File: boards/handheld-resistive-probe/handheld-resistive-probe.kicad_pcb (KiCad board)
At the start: 4 copper layers, 75 x 8 mm, 4 parts, among them J1 Conn_Coaxial, J2 Conn_01x01

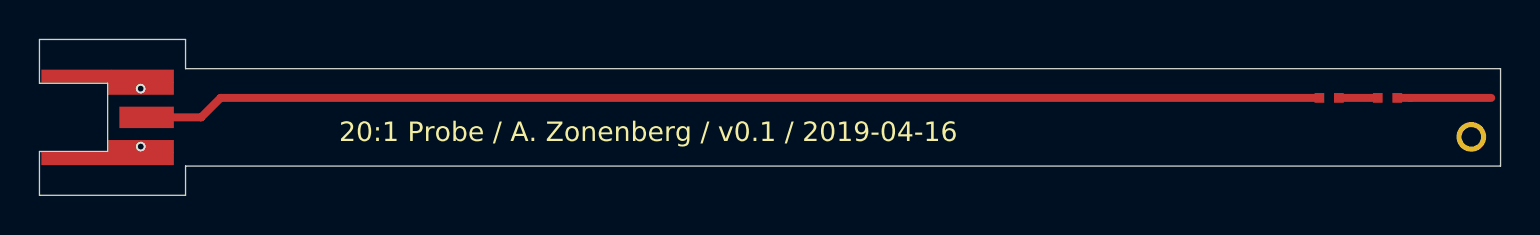
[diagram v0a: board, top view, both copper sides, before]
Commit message: handheld-resistive-probe: respin with coplanar waveguide PCB layout
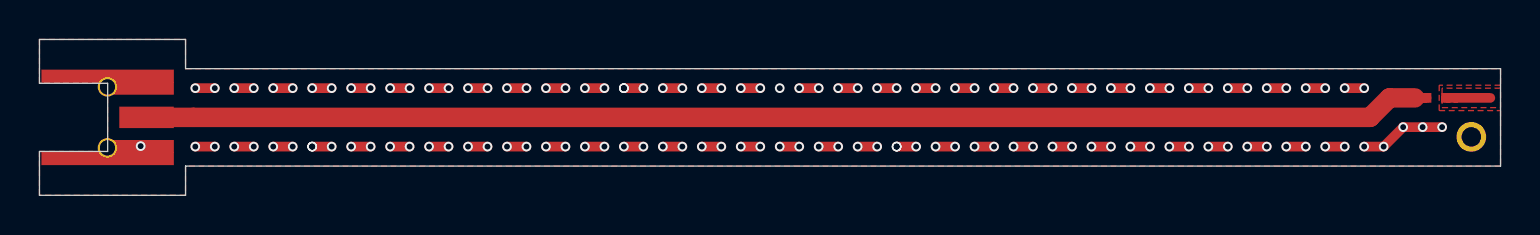
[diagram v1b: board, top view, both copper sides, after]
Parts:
- removed R2: 475, azonenberg_pcb:EIA_0402_RES_NOSILK
- R1: value 475 -> 953
- moved R1 5.50 mm to (86.7, 23.5)
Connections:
- net Net-(J1-Pad1) renamed /SIGNAL
- R1 pad 1: Net-(R1-Pad1) -> /PROBE
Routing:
- net /GND: track 76.4 -> 139.1 mm, vias 2 -> 130
- net /SIGNAL: track 60.6 -> 66.1 mm
- net Net-(R2-Pad1): track 4.82 -> 0.00 mm
- net /PROBE: track 0.00 -> 2.27 mm
- net Net-(R1-Pad1): track 2.00 -> 0.00 mm
- added copper zone on F.Cu, net /GND
- added copper zone on In2.Cu, net /GND
- added copper zone on F.Cu, net /PROBE
- removed copper zone on In1.Cu, net /GND
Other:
- net class Default: clearance 0.25 -> 0.125; trace_width 0.41 -> 1
- rule trace_clearance: 0.25 -> 0.125
- board text added: "20:1 Probe / A. Zonenberg / v0.2 / 2019-05-09"
- board text removed: "20:1 Probe / A. Zonenberg / v0.1 / 2019-04-16"

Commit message: New rev of handheld-resistive-probe with five resistors to reduce parasitics
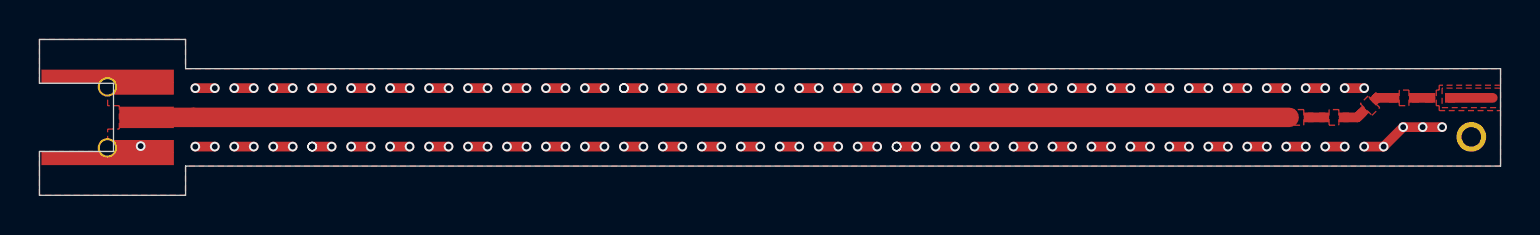
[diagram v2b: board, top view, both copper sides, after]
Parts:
- added R2: 100, azonenberg_pcb:EIA_0402_RES_NOSILK, F.Cu at (81.5, 24.5)
- added R3: 100, azonenberg_pcb:EIA_0402_RES_NOSILK, F.Cu at (83.2, 23.9)
- added R4: 100, azonenberg_pcb:EIA_0402_RES_NOSILK, F.Cu at (85.0, 23.5)
- added R5: 100, azonenberg_pcb:EIA_0402_RES_NOSILK, F.Cu at (86.9, 23.5)
- R1: value 953 -> 50
- moved R1 7.12 mm to (79.7, 24.5)
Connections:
- R1 pad 1: /PROBE -> Net-(R1-Pad1)
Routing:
- net /SIGNAL: track 66.1 -> 58.7 mm
- net Net-(R2-Pad1): track 0.00 -> 1.05 mm
- net Net-(R?1560907537-Pad1): track 0.00 -> 0.97 mm
- net Net-(R?1560908546-Pad1): track 0.00 -> 0.85 mm
- net Net-(R1-Pad1): track 0.00 -> 0.80 mm
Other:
- outline, holes or cut-outs redrawn
- board text added: "20:1 Probe / A. Zonenberg / v0.3 / 2019-06-18"
- board text removed: "20:1 Probe / A. Zonenberg / v0.2 / 2019-05-09"

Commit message: Added distributed-element compensation cap for v0.4
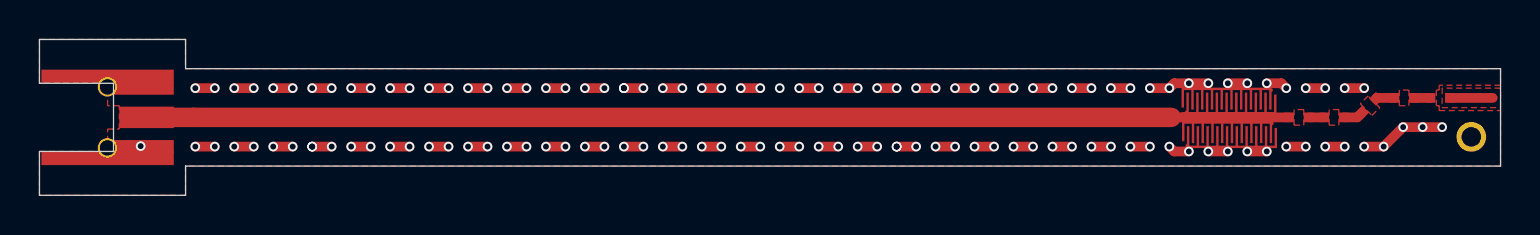
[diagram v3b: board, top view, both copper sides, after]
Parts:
- added C1: 500 fF, azonenberg_pcb:CAP_MICROSTRIP_0p5PF, F.Cu at (73.9, 25.9)
- added C2: 500 fF, azonenberg_pcb:CAP_MICROSTRIP_0p5PF, F.Cu at (78.2, 23.1)
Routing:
- net /GND: track 139.1 -> 141.6 mm
- net /SIGNAL: track 58.7 -> 59.7 mm
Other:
- rule trace_min: 0.2 -> 0.125
- board text added: "20:1 Probe / A. Zonenberg / v0.4 / 2019-06-21"
- board text removed: "20:1 Probe / A. Zonenberg / v0.3 / 2019-06-18"

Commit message: Updated handheld-resistive-probe for increased line impedance
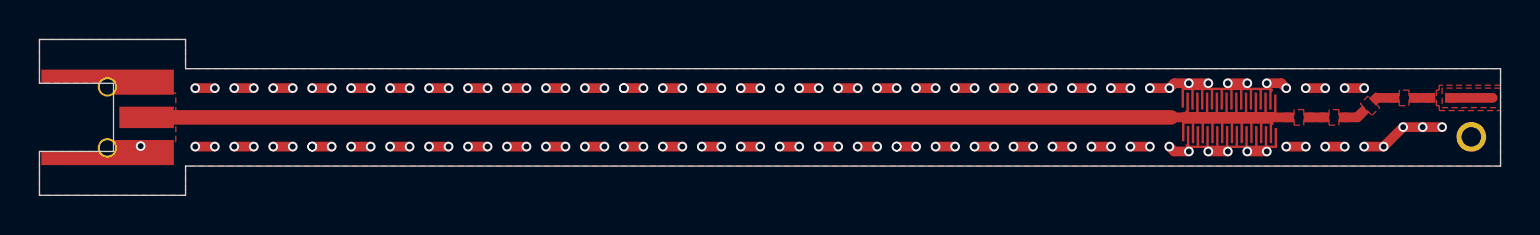
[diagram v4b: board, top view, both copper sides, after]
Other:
- board text added: "20:1 Probe / A. Zonenberg / v0.5 / 2019-07-02"
- board text removed: "20:1 Probe / A. Zonenberg / v0.4 / 2019-06-21"
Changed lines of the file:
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@@
     (thickness 1.6)
     (drawings 13)
-    (tracks 295)
+    (tracks 294)
     (modules 9)
     (nets 8)
@@
   )
   (setup
-    (last_trace_width 0.125)
+    (last_trace_width 1)
     (user_trace_width 0.125)
     (user_trace_width 0.5)
     (user_trace_width 1)
     (trace_clearance 0.125)
-    (zone_clearance 0.125)
+    (zone_clearance 0.2)
     (zone_45_only no)
     (trace_min 0.125)
@@
     )
   )
-  (gr_text "20:1 Probe / A. Zonenberg / v0.4 / 2019-06-21" (at 51.75 24.65) (layer "B.SilkS")
+  (gr_text "20:1 Probe / A. Zonenberg / v0.5 / 2019-07-02" (at 51.75 24.65) (layer "B.SilkS")
     (effects (font (size 1 1) (thickness 0.125)) (justify mirror))
   )
@@
   (gr_line (start 90 22) (end 22.5 22) (layer "Edge.Cuts") (width 0.05))
   (gr_line (start 90 22) (end 90 27) (layer "Edge.Cuts") (width 0.05))
-  (segment (start 18.698826 26.73001) (end 18.5 26.73001) (width 0.41) (layer "F.Cu") (net 1))
-  (segment (start 20.195 26.6975) (end 20.16249 26.73001) (width 0.41) (layer "F.Cu") (net 1))
-  (segment (start 20.16249 26.73001) (end 18.698826 26.73001) (width 0.41) (layer "F.Cu") (net 1))
-  (segment (start 20.195 25.975) (end 20.195 26.6975) (width 0.41) (layer "F.Cu") (net 1))
+  (segment (start 18.698826 26.73001) (end 18.5 26.73001) (width 0.41) (layer "F.Cu") (net 1) (status 30))
+  (segment (start 20.195 26.6975) (end 20.16249 26.73001) (width 0.41) (layer "F.Cu") (net 1) (status 30))
+  (segment (start 20.16249 26.73001) (end 18.698826 26.73001) (width 0.41) (layer "F.Cu") (net 1) (status 30))
+  (segment (start 20.195 25.975) (end 20.195 26.6975) (width 0.41) (layer "F.Cu") (net 1) (status 30))
   (via (at 77 26.25) (size 0.5) (drill 0.3) (layers "F.Cu" "B.Cu") (net 1))
   (segment (start 78 26.25) (end 77 26.25) (width 0.5) (layer "F.Cu") (net 1))
@@
   (via (at 23 26) (size 0.5) (drill 0.3) (layers "F.Cu" "B.Cu") (net 1))
   (segment (start 24 26) (end 23 26) (width 0.5) (layer "F.Cu") (net 1))
-  (via (at 20.195 25.975) (size 0.5) (drill 0.3) (layers "F.Cu" "B.Cu") (net 1))
+  (via (at 20.195 25.975) (size 0.5) (drill 0.3) (layers "F.Cu" "B.Cu") (net 1) (status 30))
   (segment (start 20.22 26) (end 20.195 25.975) (width 0.5) (layer "In2.Cu") (net 1))
   (segment (start 23 26) (end 20.22 26) (width 0.5) (layer "In2.Cu") (net 1))
@@
   (segment (start 82 23) (end 83 23) (width 0.5) (layer "F.Cu") (net 1))
   (via (at 85 25) (size 0.5) (drill 0.3) (layers "F.Cu" "B.Cu") (net 1))
-  (segment (start 88 25) (end 88.5 25.5) (width 0.5) (layer "In2.Cu") (net 1))
+  (segment (start 88 25) (end 88.5 25.5) (width 0.5) (layer "In2.Cu") (net 1) (status 30))
   (via (at 86 25) (size 0.5) (drill 0.3) (layers "F.Cu" "B.Cu") (net 1))
   (segment (start 85 25) (end 86 25) (width 0.5) (layer "F.Cu") (net 1))
@@
   (segment (start 86 25) (end 87 25) (width 0.5) (layer "F.Cu") (net 1))
   (via (at 87 25) (size 0.5) (drill 0.3) (layers "F.Cu" "B.Cu") (net 1))
-  (segment (start 87 25) (end 88 25) (width 0.5) (layer "In2.Cu") (net 1))
+  (segment (start 87 25) (end 88 25) (width 0.5) (layer "In2.Cu") (net 1) (status 20))
   (segment (start 86 25) (end 87 25) (width 0.5) (layer "In2.Cu") (net 1))
   (segment (start 73.9 26.15) (end 74 26.25) (width 0.125) (layer "F.Cu") (net 1))
-  (segment (start 19.854999 22.247499) (end 18.820001 22.247499) (width 0.125) (layer "F.Cu") (net 1))
-  (segment (start 20.195 22.5875) (end 19.854999 22.247499) (width 0.125) (layer "F.Cu") (net 1))
-  (segment (start 20.195 23.025) (end 20.195 22.5875) (width 0.125) (layer "F.Cu") (net 1))
+  (segment (start 19.854999 22.247499) (end 18.820001 22.247499) (width 0.125) (layer "F.Cu") (net 1) (status 30))
+  (segment (start 20.195 22.5875) (end 19.854999 22.247499) (width 0.125) (layer "F.Cu") (net 1) (status 30))
+  (segment (start 20.195 23.025) (end 20.195 22.5875) (width 0.125) (layer "F.Cu") (net 1) (status 30))
   (segment (start 78.75 22.75) (end 79 23) (width 0.5) (layer "F.Cu") (net 1))
   (segment (start 78 22.75) (end 78.75 22.75) (width 0.5) (layer "F.Cu") (net 1))
@@
   (segment (start 78.75 26.25) (end 79 26) (width 0.5) (layer "In2.Cu") (net 1))
   (segment (start 78 26.25) (end 78.75 26.25) (width 0.5) (layer "In2.Cu") (net 1))
-  (segment (start 87.4 23.5) (end 89.59999 23.5) (width 0.5) (layer "F.Cu") (net 2))
-  (segment (start 22.9 24.5) (end 20.5 24.5) (width 1) (layer "F.Cu") (net 3))
-  (segment (start 80.95 24.5) (end 80.15 24.5) (width 0.5) (layer "F.Cu") (net 4))
-  (segment (start 83.65 23.5) (end 83.603553 23.546447) (width 0.5) (layer "F.Cu") (net 5))
-  (segment (start 84.55 23.5) (end 83.65 23.5) (width 0.5) (layer "F.Cu") (net 5))
-  (segment (start 85.55 23.5) (end 86.4 23.5) (width 0.5) (layer "F.Cu") (net 6))
-  (segment (start 82.65 24.5) (end 82.896447 24.253553) (width 0.5) (layer "F.Cu") (net 7))
-  (segment (start 81.95 24.5) (end 82.65 24.5) (width 0.5) (layer "F.Cu") (net 7))
-  (segment (start 79.15 24.5) (end 79.1 24.5) (width 0.125) (layer "F.Cu") (net 3))
-  (segment (start 79.075 24.575) (end 79.15 24.5) (width 0.125) (layer "F.Cu") (net 3))
-  (segment (start 22.9 24.5) (end 73.1 24.5) (width 1) (layer "F.Cu") (net 3))
+  (segment (start 87.4 23.5) (end 89.59999 23.5) (width 0.5) (layer "F.Cu") (net 2) (status 10))
+  (segment (start 73.1 24.5) (end 20.5 24.5) (width 0.75) (layer "F.Cu") (net 3) (status 20))
+  (segment (start 79.15 24.5) (end 79.1 24.5) (width 0.125) (layer "F.Cu") (net 3) (status 30))
+  (segment (start 79.075 24.575) (end 79.15 24.5) (width 0.125) (layer "F.Cu") (net 3) (status 30))
   (segment (start 73.175 24.425) (end 73 24.6) (width 0.125) (layer "F.Cu") (net 3))
   (segment (start 73.1 24.5) (end 73.7 24.5) (width 0.5) (layer "F.Cu") (net 3))
   (segment (start 78.275 24.6625) (end 78.25 24.6375) (width 0.125) (layer "F.Cu") (net 3))
-  (segment (start 78.275 24.825) (end 78.275 24.6625) (width 0.125) (layer "F.Cu") (net 3))
+  (segment (start 78.275 24.825) (end 78.275 24.6625) (width 0.125) (layer "F.Cu") (net 3) (status 10))
   (segment (start 78.25 24.6375) (end 78.25 24.5) (width 0.125) (layer "F.Cu") (net 3))
   (segment (start 73.7 24.5) (end 78.25 24.5) (width 0.5) (layer "F.Cu") (net 3))
-  (segment (start 78.25 24.5) (end 79.15 24.5) (width 0.5) (layer "F.Cu") (net 3))
+  (segment (start 78.25 24.5) (end 79.15 24.5) (width 0.5) (layer "F.Cu") (net 3) (status 20))
   (segment (start 73.7 24.4) (end 73.7 24.5) (width 0.125) (layer "F.Cu") (net 3))
-  (segment (start 73.875 24.225) (end 73.7 24.4) (width 0.125) (layer "F.Cu") (net 3))
+  (segment (start 73.875 24.225) (end 73.7 24.4) (width 0.125) (layer "F.Cu") (net 3) (status 10))
+  (segment (start 80.95 24.5) (end 80.15 24.5) (width 0.5) (layer "F.Cu") (net 4) (status 30))
+  (segment (start 83.65 23.5) (end 83.603553 23.546447) (width 0.5) (layer "F.Cu") (net 5) (status 30))
+  (segment (start 84.55 23.5) (end 83.65 23.5) (width 0.5) (layer "F.Cu") (net 5) (status 30))
+  (segment (start 85.55 23.5) (end 86.4 23.5) (width 0.5) (layer "F.Cu") (net 6) (status 30))
+  (segment (start 82.65 24.5) (end 82.896447 24.253553) (width 0.5) (layer "F.Cu") (net 7) (status 20))
+  (segment (start 81.95 24.5) (end 82.65 24.5) (width 0.5) (layer "F.Cu") (net 7) (status 10))
   (zone (net 2) (net_name "/PROBE") (layer "F.Cu") (hatch edge 0.508)
     (connect_pads yes (clearance 0.125))
@@
   )
   (zone (net 1) (net_name "/GND") (layer "F.Cu") (hatch edge 0.508)
-    (connect_pads yes (clearance 0.125))
-    (min_thickness 0.125)
+    (connect_pads yes (clearance 0.2))
+    (min_thickness 0.2)
     (fill yes (arc_segments 32) (thermal_gap 0.1) (thermal_bridge_width 0.508))
     (polygon
@@
         (xy 86.7 23.1) (xy 86.7 23.9) (xy 86.85 23.9) (xy 86.85 24.15) (xy 90 24.15)
         (xy 90 27) (xy 22.5 27) (xy 22.5 28.5) (xy 15 28.5) (xy 15 26.25)
-        (xy 18.5 26.25) (xy 18.5 25.1) (xy 19.1 25.1) (xy 19.1 23.9) (xy 18.5 23.9)
+        (xy 18.5 26.25) (xy 18.5 25.75) (xy 22 25.75) (xy 22 23.25) (xy 18.5 23.25)
         (xy 18.5 22.75) (xy 15 22.75) (xy 15 20.5) (xy 22.5 20.5)
       )
